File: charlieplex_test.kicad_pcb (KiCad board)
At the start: 2 copper layers, 38 x 60 mm, 212 parts, among them J1 external, SW1 SW_SPDT, U1 CH32V003FxPx, U2 TPS61221DCK

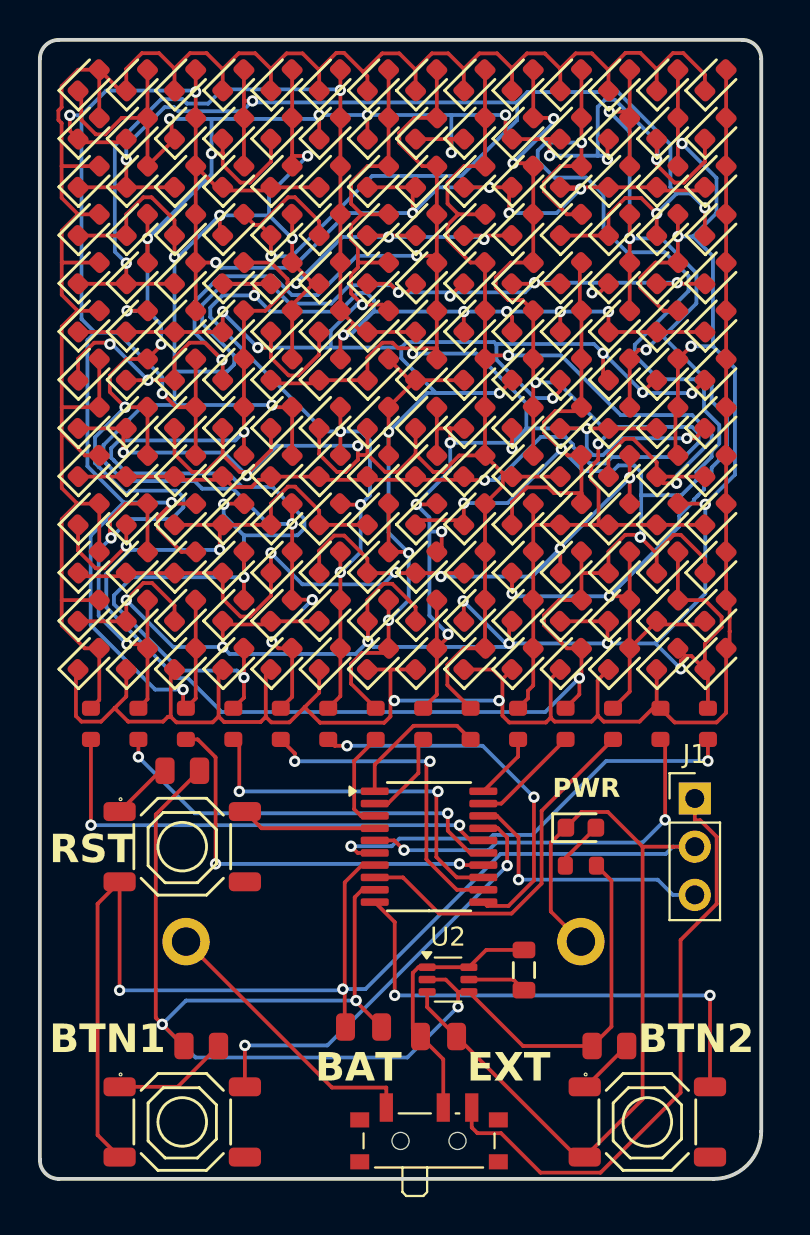
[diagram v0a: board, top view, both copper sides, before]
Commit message: Improved layout of power supply actually work- added block capacitor to the uC as well as ground planes
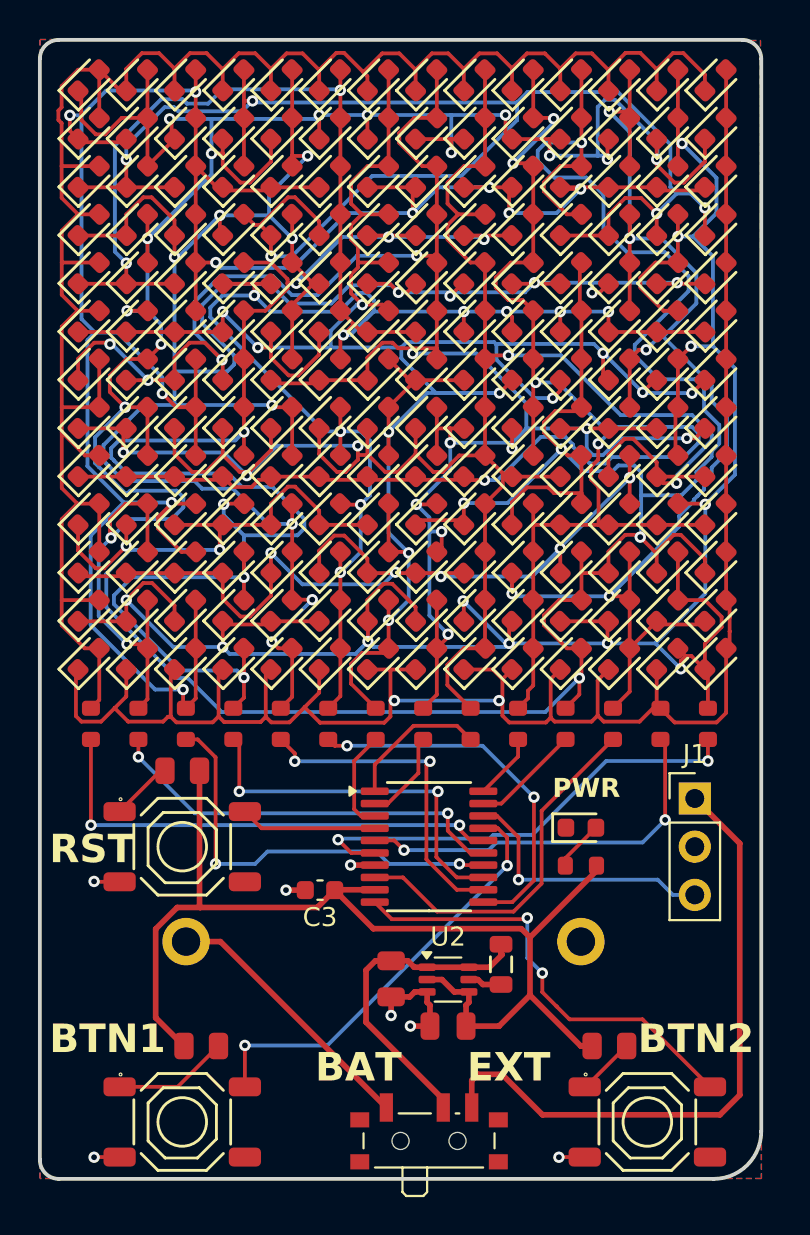
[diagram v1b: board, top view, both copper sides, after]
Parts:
- added C3: 100n, Capacitor_SMD:C_0603_1608Metric, F.Cu at (75.8, 72.3)
- moved C2 4.45 mm to (82.5, 79.5)
- moved C1 3.93 mm to (79.5, 77.0), turned to -90 degrees
- moved L1 1.24 mm to (85.3, 76.2)
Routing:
- net GND: track 109.2 -> 12.2 mm, vias 2 -> 7
- net 3V3: track 74.0 -> 58.7 mm, vias 3 -> 0
- net PC0: track 26.8 -> 23.6 mm
- net Net-(SW1-B): track 14.1 -> 17.3 mm
- net Net-(J1-Pin_1): track 31.7 -> 33.6 mm
- net PA2: track 23.2 -> 24.6 mm
- net Net-(U2-L): track 3.13 -> 1.80 mm
- net /VBAT: track 14.8 -> 14.2 mm
- net PC4: track 21.7 -> 22.2 mm
- added copper zone on B.Cu, net GND
- added copper zone on F.Cu, net GND
